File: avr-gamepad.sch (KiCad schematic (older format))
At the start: 33 parts, among them J1 Conn_01x08, J2 Conn_01x08, P1 USB_C_Plug_USB2.0, SW1 RESET, SW10 Up, SW11 Down, SW12 Left, SW13 Select, SW14 HWB, SW2 R, SW3 X, SW4 A, SW5 B, SW6 Start, SW7 Y, SW8 Right, SW9 L, U1 ATmega32U4-AU, Y1 Crystal_GND24

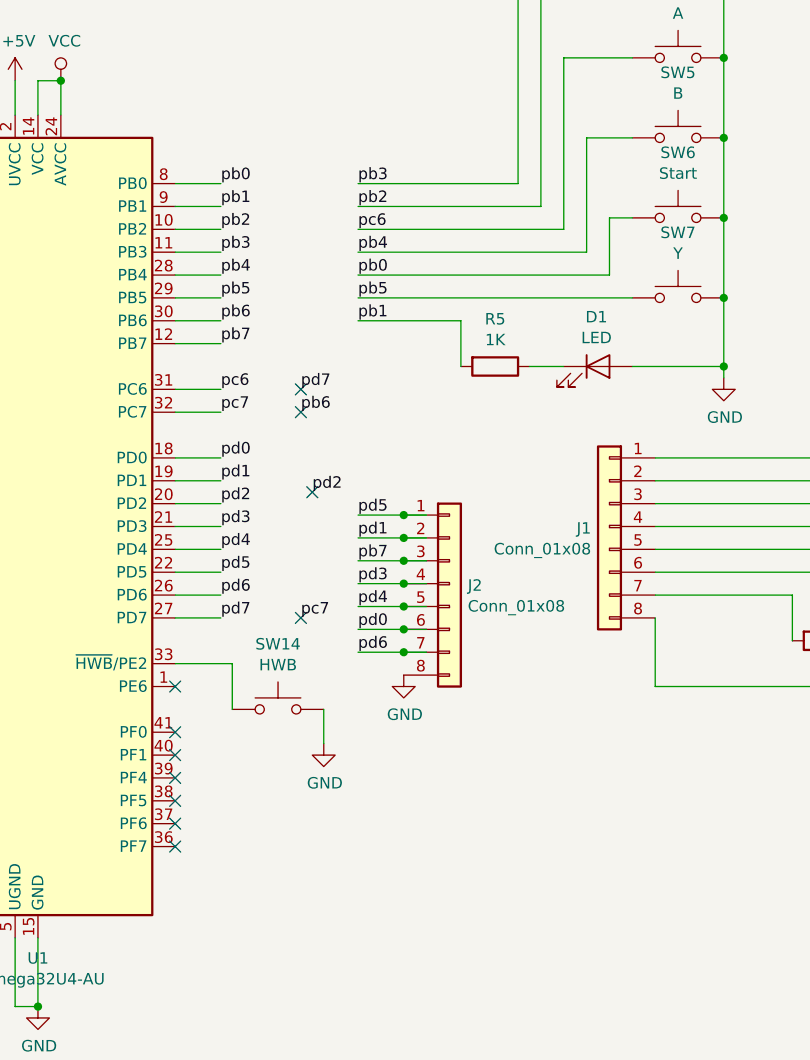
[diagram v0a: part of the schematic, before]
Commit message: add 0.1 in headers, label atmega pins better
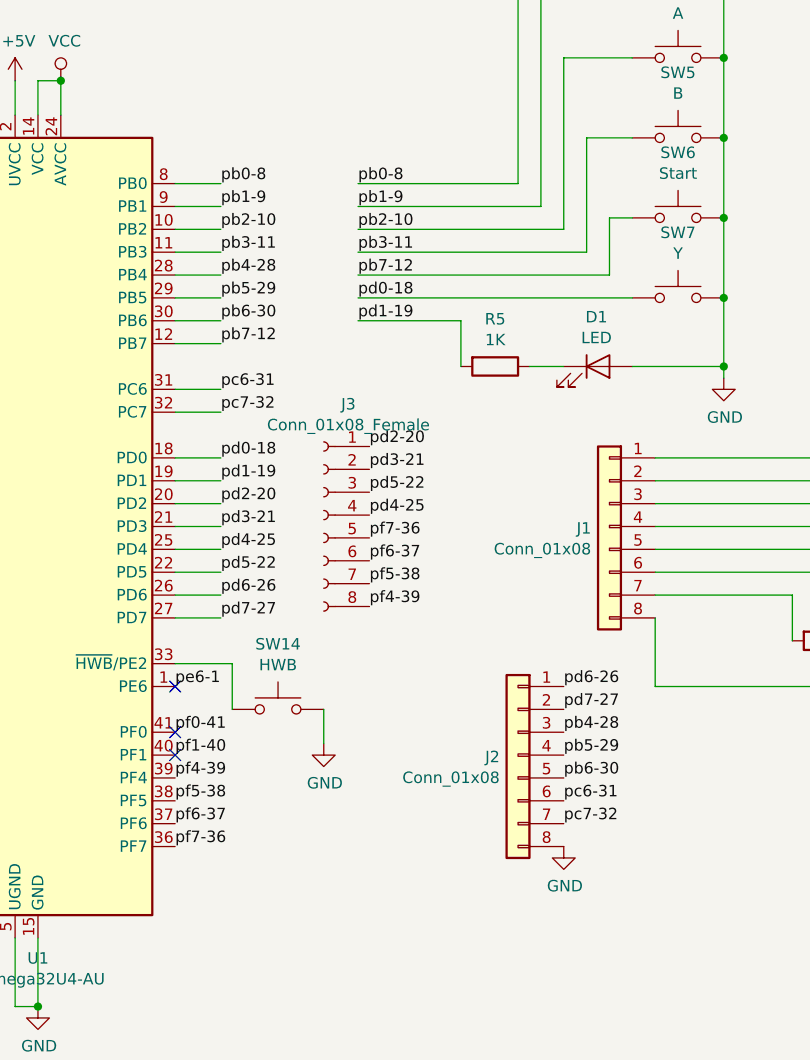
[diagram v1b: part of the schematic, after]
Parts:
- added J3: Conn_01x08_Female, Connector_PinHeader_2.54mm:PinHeader_1x08_P2.54mm_Vertical, symbol Connector:Conn_01x08_Female
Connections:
- net labels added: pb0-8, pb1-9, pb2-10, pb3-11, pb4-28, pb5-29, pb6-30, pb7-12, pc6-31, pc7-32, pd0-18, pd1-19, pd2-20, pd3-21, pd4-25, pd5-22, pd6-26, pd7-27, pe6-1, pf0-41, pf1-40, pf4-39, pf5-38, pf6-37, pf7-36
- net labels removed: pb0, pb1, pb2, pb3, pb4, pb5, pb6, pb7, pc6, pc7, pd0, pd1, pd2, pd3, pd4, pd5, pd6, pd7
- wire segments 153 -> 139
- no-connect marks 11 -> 3
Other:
- moved on the sheet: J2
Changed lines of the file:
@@
 Connection ~ 7500 2600
 Connection ~ 7500 2900
-NoConn ~ 5100 4500
-NoConn ~ 5100 4600
-NoConn ~ 5100 4700
-NoConn ~ 5100 4800
-NoConn ~ 5100 4900
-NoConn ~ 5100 5000
 $Comp
 L power:GND #PWR01
@@
 Wire Wire Line
 	1400 4400 1400 4550
-Wire Wire Line
-	5900 4150 6100 4150
-Wire Wire Line
-	5900 4050 6100 4050
-Wire Wire Line
-	5900 3950 6100 3950
-Wire Wire Line
-	5900 3850 6100 3850
-Wire Wire Line
-	5900 3750 6100 3750
-Wire Wire Line
-	5900 3650 6100 3650
-Wire Wire Line
-	5900 3550 6100 3550
 Text Label 5300 2800 0    50   ~ 0
-pb7
+pb7-12
 Text Label 5300 2700 0    50   ~ 0
-pb6
+pb6-30
 Text Label 5300 2600 0    50   ~ 0
-pb5
+pb5-29
 Text Label 5300 2500 0    50   ~ 0
-pb4
+pb4-28
 Text Label 5300 2400 0    50   ~ 0
-pb3
+pb3-11
 Text Label 5300 2300 0    50   ~ 0
-pb2
+pb2-10
 Text Label 5300 2200 0    50   ~ 0
-pb1
+pb1-9
 Text Label 5300 2100 0    50   ~ 0
-pb0
+pb0-8
 Wire Wire Line
 	5100 2100 5300 2100
@@
 Wire Wire Line
 	5100 2800 5300 2800
-Text Label 5900 2700 0    50   ~ 0
-pb1
-Text Label 5900 2200 0    50   ~ 0
-pb2
-Text Label 5900 2400 0    50   ~ 0
-pb4
-Text Label 5900 2600 0    50   ~ 0
-pb5
-Text Label 5900 3650 0    50   ~ 0
-pd1
-Text Label 5700 3450 0    50   ~ 0
-pd2
-Text Label 5900 3850 0    50   ~ 0
-pd3
-Text Label 5900 3950 0    50   ~ 0
-pd4
-Text Label 5900 3550 0    50   ~ 0
-pd5
-Text Label 5650 3000 0    50   ~ 0
-pd7
+Text Label 6800 4500 0    50   ~ 0
+pb4-28
 Text Label 5300 3300 0    50   ~ 0
-pd0
+pd0-18
 Text Label 5300 3400 0    50   ~ 0
-pd1
+pd1-19
 Text Label 5300 3500 0    50   ~ 0
-pd2
+pd2-20
 Text Label 5300 3600 0    50   ~ 0
-pd3
+pd3-21
 Text Label 5300 3700 0    50   ~ 0
-pd4
+pd4-25
 Text Label 5300 3800 0    50   ~ 0
-pd5
+pd5-22
 Text Label 5300 3900 0    50   ~ 0
-pd6
+pd6-26
 Wire Wire Line
 	5100 3300 5300 3300
@@
 Wire Wire Line
 	5100 3900 5300 3900
-NoConn ~ 5700 3450
-Text Label 5900 3750 0    50   ~ 0
-pb7
-NoConn ~ 5100 4300
 Text Label 5300 4000 0    50   ~ 0
-pd7
+pd7-27
 Wire Wire Line
 	5300 4000 5100 4000
 Text Label 5300 3100 0    50   ~ 0
-pc7
+pc7-32
 Wire Wire Line
 	5300 3100 5100 3100
 Text Label 5300 3000 0    50   ~ 0
-pc6
+pc6-31
 Wire Wire Line
 	5300 3000 5100 3000
-Text Label 5900 2300 0    50   ~ 0
-pc6
-Text Label 5650 3100 0    50   ~ 0
-pb6
-NoConn ~ 5650 3100
 Wire Wire Line
 	1100 4400 1100 4550
@@
 	1    0    0    -1
 $EndComp
-Text Label 5900 4150 0    50   ~ 0
-pd6
-NoConn ~ 5650 3000
-NoConn ~ 5650 4000
-Text Label 5650 4000 0    50   ~ 0
-pc7
-Text Label 5900 2500 0    50   ~ 0
-pb0
+Text Label 6800 4300 0    50   ~ 0
+pd6-26
 Wire Wire Line
 	8050 2050 8550 2050
@@
 	1    0    0    -1
 $EndComp
-Text Label 5900 2100 0    50   ~ 0
-pb3
-Text Label 5900 4050 0    50   ~ 0
-pd0
 $Comp
 L Switch:SW_Push SW1
@@
 L Connector_Generic:Conn_01x08 J2
 U 1 1 5D94373B
-P 6300 3850
-F 0 "J2" H 6380 3842 50  0000 L CNN
-F 1 "Conn_01x08" H 6380 3751 50  0000 L CNN
-F 2 "Connector_FFC-FPC:Hirose_FH12-8S-0.5SH_1x08-1MP_P0.50mm_Horizontal" H 6300 3850 50  0001 C CNN
-F 3 "~" H 6300 3850 50  0001 C CNN
-	1    6300 3850
-	1    0    0    -1
-$EndComp
-Connection ~ 6100 3550
-Wire Wire Line
-	6100 3550 6200 3550
-Connection ~ 6100 3650
-Wire Wire Line
-	6100 3650 6200 3650
-Connection ~ 6100 3750
-Wire Wire Line
-	6100 3750 6200 3750
-Connection ~ 6100 3850
-Wire Wire Line
-	6100 3850 6200 3850
-Connection ~ 6100 3950
-Wire Wire Line
-	6100 3950 6200 3950
-Connection ~ 6100 4050
-Wire Wire Line
-	6100 4050 6200 4050
-Connection ~ 6100 4150
-Wire Wire Line
-	6100 4150 6200 4150
+P 6600 4600
+F 0 "J2" H 6680 4592 50  0000 L CNN
+F 1 "Conn_01x08" H 6680 4501 50  0000 L CNN
+F 2 "Connector_FFC-FPC:Hirose_FH12-8S-0.5SH_1x08-1MP_P0.50mm_Horizontal" H 6600 4600 50  0001 C CNN
+F 3 "~" H 6600 4600 50  0001 C CNN
+	1    6600 4600
+	-1   0    0    -1
+$EndComp
 Wire Wire Line
 	7200 3900 7800 3900
@@
 L power:GND #PWR0113
 U 1 1 5D9668CC
-P 6100 4250
-F 0 "#PWR0113" H 6100 4000 50  0001 C CNN
-F 1 "GND" H 6105 4077 50  0000 C CNN
-F 2 "" H 6100 4250 50  0001 C CNN
-F 3 "" H 6100 4250 50  0001 C CNN
-	1    6100 4250
+P 6800 5000
+F 0 "#PWR0113" H 6800 4750 50  0001 C CNN
+F 1 "GND" H 6805 4827 50  0000 C CNN
+F 2 "" H 6800 5000 50  0001 C CNN
+F 3 "" H 6800 5000 50  0001 C CNN
+	1    6800 5000
 	1    0    0    -1
 $EndComp
@@
 Wire Wire Line
 	5750 4550 5750 4400
+Text Label 5100 4500 0    50   ~ 0
+pf0-41
+Text Label 5100 4600 0    50   ~ 0
+pf1-40
+Text Label 5100 4700 0    50   ~ 0
+pf4-39
+Text Label 5100 4800 0    50   ~ 0
+pf5-38
+Text Label 5100 4900 0    50   ~ 0
+pf6-37
+Text Label 5100 5000 0    50   ~ 0
+pf7-36
+Text Label 5100 4300 0    50   ~ 0
+pe6-1
+$Comp
+L Connector:Conn_01x08_Female J3
+U 1 1 5DA62D9E
+P 5750 3550
+F 0 "J3" H 5642 4035 50  0000 C CNN
+F 1 "Conn_01x08_Female" H 5642 3944 50  0000 C CNN
+F 2 "Connector_PinHeader_2.54mm:PinHeader_1x08_P2.54mm_Vertical" H 5750 3550 50  0001 C CNN
+F 3 "~" H 5750 3550 50  0001 C CNN
+	1    5750 3550
+	-1   0    0    -1
+$EndComp
+Text Label 6800 4900 0    50   ~ 0
+pc7-32
+Text Label 6800 4800 0    50   ~ 0
+pc6-31
+Text Label 6800 4700 0    50   ~ 0
+pb6-30
+Text Label 6800 4600 0    50   ~ 0
+pb5-29
+Text Label 6800 4400 0    50   ~ 0
+pd7-27
+Text Label 5950 3550 0    50   ~ 0
+pd4-25
+Text Label 5950 3350 0    50   ~ 0
+pd3-21
+Text Label 5950 3250 0    50   ~ 0
+pd2-20
+Text Label 5950 3450 0    50   ~ 0
+pd5-22
+Text Label 5900 2700 0    50   ~ 0
+pd1-19
+Text Label 5900 2600 0    50   ~ 0
+pd0-18
+Text Label 5900 2500 0    50   ~ 0
+pb7-12
+Text Label 5900 2400 0    50   ~ 0
+pb3-11
+Text Label 5950 3650 0    50   ~ 0
+pf7-36
+Text Label 5950 3850 0    50   ~ 0
+pf5-38
+Text Label 5950 3950 0    50   ~ 0
+pf4-39
+NoConn ~ 5100 4500
+NoConn ~ 5100 4600
+Text Label 5900 2300 0    50   ~ 0
+pb2-10
+Text Label 5900 2200 0    50   ~ 0
+pb1-9
+Text Label 5900 2100 0    50   ~ 0
+pb0-8
+NoConn ~ 5100 4300
+Text Label 5950 3750 0    50   ~ 0
+pf6-37
 $EndSCHEMATC

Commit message: savepoint
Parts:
- C3, C4: value 10pF -> 22pF
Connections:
- no-connect marks 3 -> 4
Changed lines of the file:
@@
 P 2800 2250
 F 0 "C3" V 2548 2250 50  0000 C CNN
-F 1 "10pF" V 2639 2250 50  0000 C CNN
+F 1 "22pF" V 2639 2250 50  0000 C CNN
 F 2 "Capacitor_SMD:C_0805_2012Metric" H 2800 2250 50  0001 C CNN
 F 3 "~" H 2800 2250 50  0001 C CNN
@@
 P 2800 2550
 F 0 "C4" V 3050 2550 50  0000 C CNN
-F 1 "10pF" V 2950 2550 50  0000 C CNN
+F 1 "22pF" V 2950 2550 50  0000 C CNN
 F 2 "Capacitor_SMD:C_0805_2012Metric" H 2800 2550 50  0001 C CNN
 F 3 "~" H 2800 2550 50  0001 C CNN
@@
 Text Label 5950 3750 0    50   ~ 0
 pf6-37
+NoConn ~ 8050 3400
 $EndSCHEMATC
